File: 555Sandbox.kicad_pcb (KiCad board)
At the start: 2 copper layers, 64.6 x 37 mm, 33 parts, among them J1 VIN, J2 Piezo, Q1 2N7000, SW1 RESET, SW2 MODE, U1 NE555P, U2 LM3914N

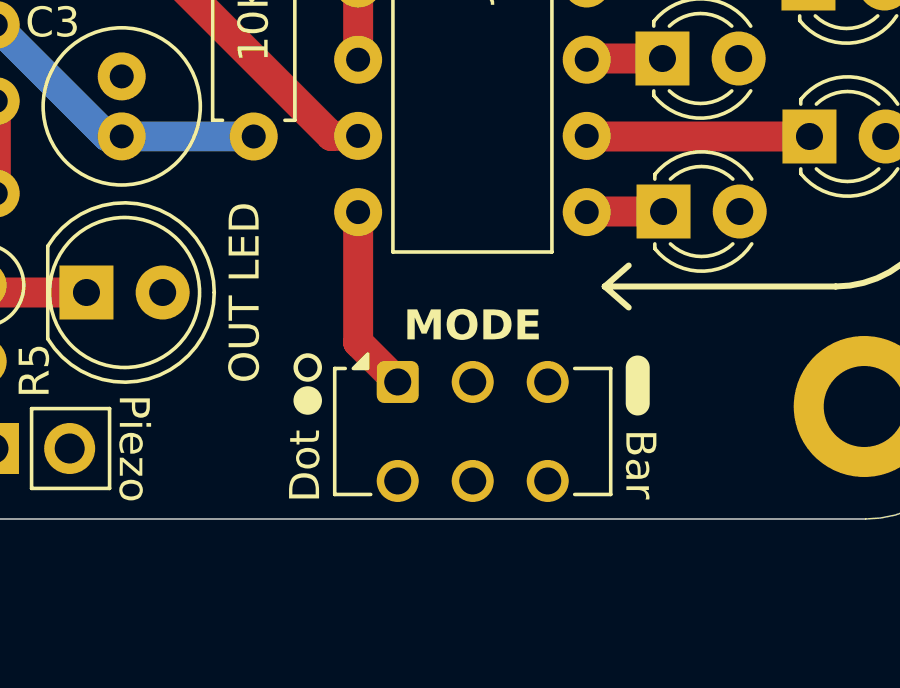
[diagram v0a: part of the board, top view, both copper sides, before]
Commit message: fix: mode switch footprint & silkscreen labels
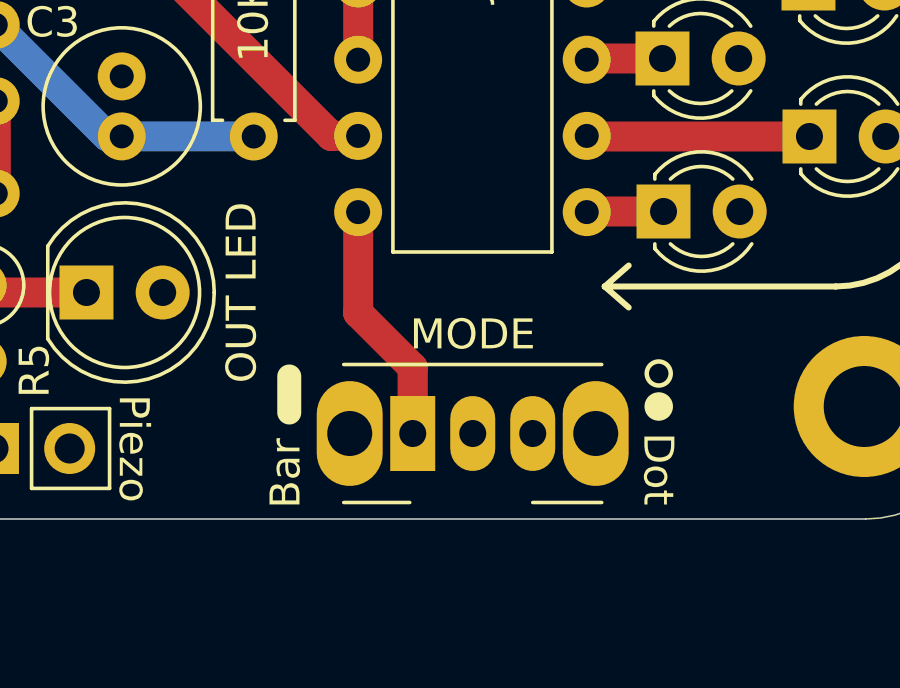
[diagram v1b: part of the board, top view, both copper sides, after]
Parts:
- SW2: footprint Button_Switch_THT:SW_CK_JS202011AQN_DPDT_Angled -> Button_Switch_THT:SW_Slide_SPDT_Angled_CK_OS102011MA1Q
- moved SW2 1.79 mm to (120.7, 98.4)
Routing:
- net Net-(SW2A-A): track 6.21 -> 8.13 mm

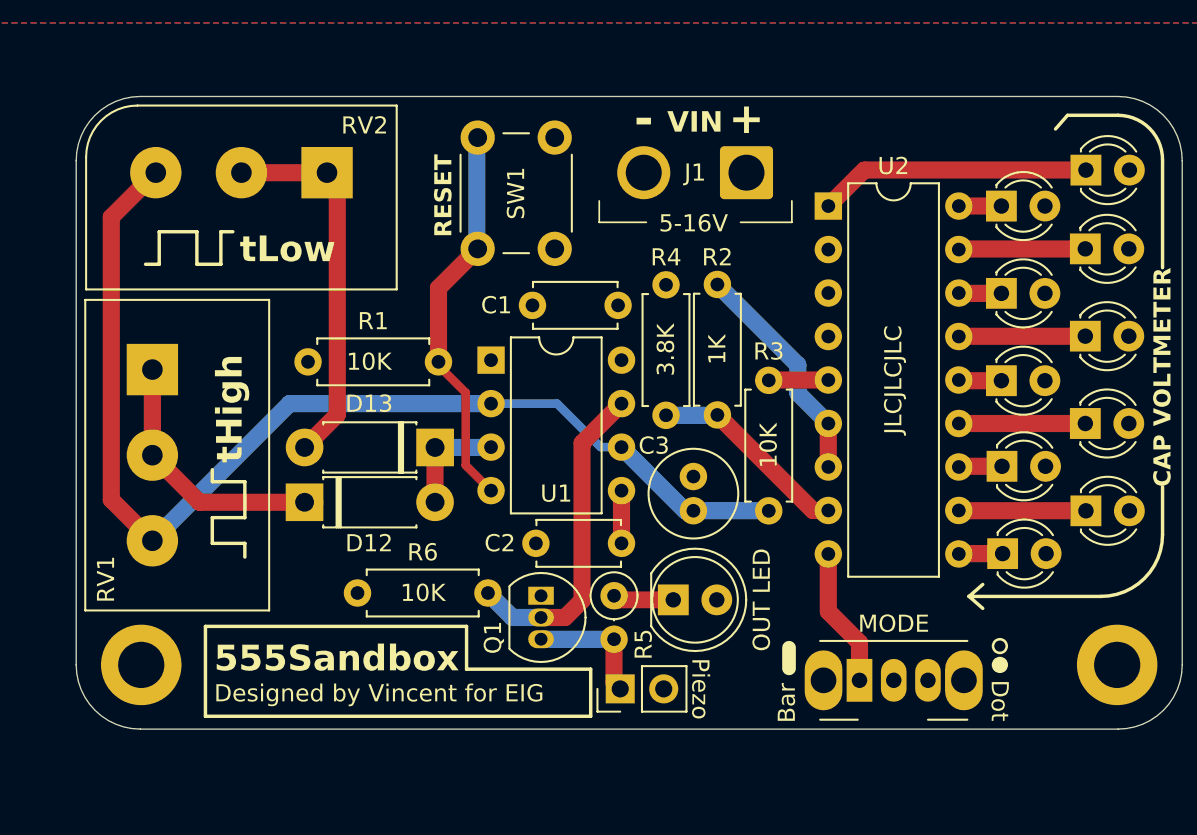
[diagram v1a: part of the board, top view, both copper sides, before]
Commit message: feat: update with separate freq and period adjustment
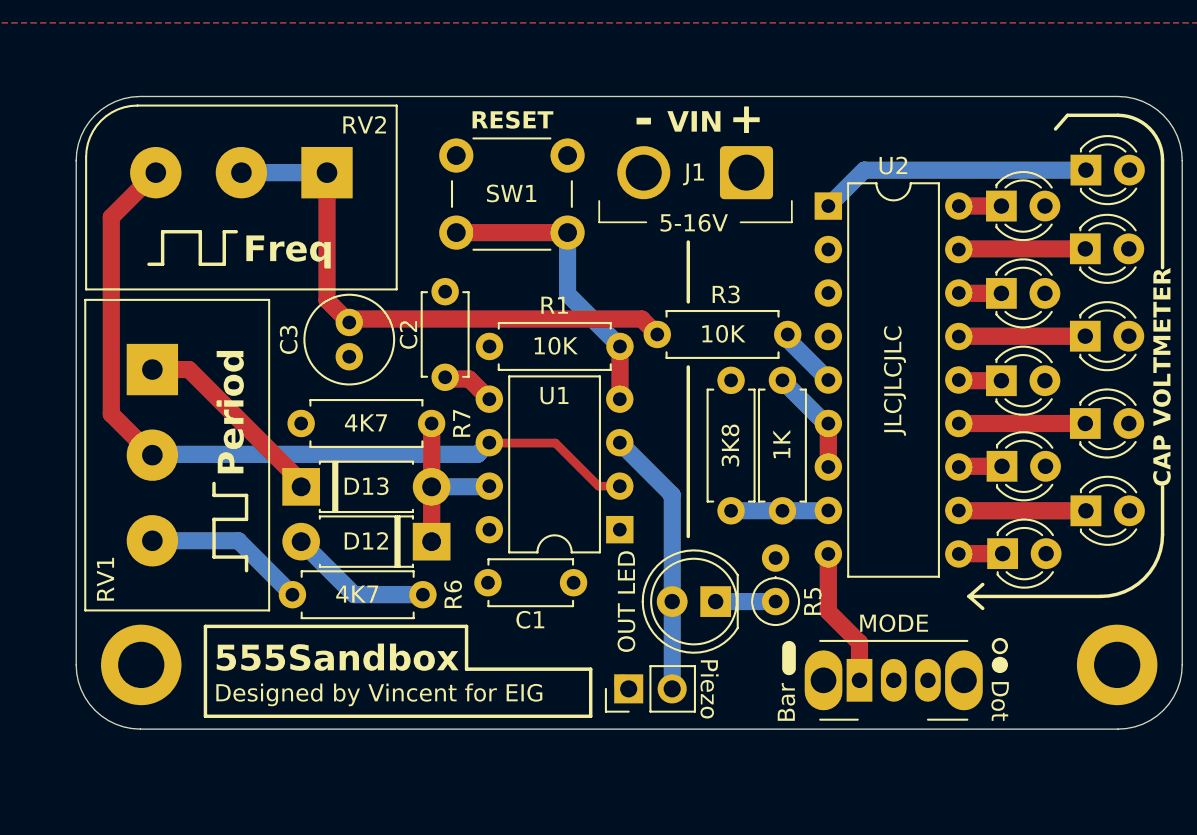
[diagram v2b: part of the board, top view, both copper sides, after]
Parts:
- removed Q1: 2N7000, Package_TO_SOT_THT:TO-92_Inline
- added R7: 4K7, Resistor_THT:R_Axial_DIN0207_L6.3mm_D2.5mm_P7.62mm_Horizontal, F.Cu at (88.1, 83.4)
- R4: value 3.8K -> 3K8
- R6: value 10K -> 4K7
- moved C3 22.9 mm to (90.9, 77.5), turned to -90 degrees
- moved C1 17.9 mm to (99.0, 92.7), turned to 0 degrees
- moved C2 14.1 mm to (96.5, 80.7), turned to 90 degrees
- moved U1 12.4 mm to (106.7, 89.6), turned to 180 degrees
- moved R3 12.2 mm to (108.9, 78.2), turned to 0 degrees
- moved R1 10.6 mm to (99.1, 78.9)
- moved R5 9.44 mm to (115.8, 93.8), turned to 90 degrees
- moved R2 6.77 mm to (116.2, 88.5)
- moved R4 6.75 mm to (113.2, 80.9)
- moved SW1 5.85 mm to (97.2, 67.8), turned to 0 degrees
- moved D13 5.50 mm to (95.7, 90.3)
- moved R6 3.82 mm to (95.2, 93.4), turned to 180 degrees
- moved D1 2.48 mm to (112.3, 93.8), turned to 180 degrees
- moved D12 0.92 mm to (88.1, 87.1)
- moved J2 0.50 mm to (107.2, 98.9)
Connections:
- C3 pad 1: /TRIG -> /VCAP
- D1 pad 2: VCC -> /OUT
- D12 pad 2: Net-(D12-A) -> /DIS
- D13 pad 1: Net-(D12-A) -> /DIS
- J2 pad 1: /OUT -> GND
- J2 pad 2: VCC -> /OUT
- R3 pad 1: /TRIG -> /VCAP
- R5 pad 2: /OUT -> GND
- R6 pad 1: VCC -> Net-(D13-A)
- R6 pad 2: /OSC_OUT -> Net-(R6-Pad2)
- RV1 pad 2: Net-(D12-K) -> /TRIG
- RV1 pad 3: /TRIG -> Net-(R6-Pad2)
- RV2 pad 1: Net-(D13-A) -> /VCAP
- RV2 pad 2: Net-(D13-A) -> /VCAP
- U1 pad 3: Net-(D12-A) -> /OUT
- U1 pad 7: /OSC_OUT -> /DIS
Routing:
- net /VCAP: track 0.00 -> 32.7 mm
- net /OSC_OUT: track 19.0 -> 0.00 mm
- net /TRIG: track 65.5 -> 47.2 mm
- net Net-(D13-A): track 22.1 -> 8.39 mm
- net /DIS: track 0.00 -> 10.3 mm
- net Net-(R6-Pad2): track 0.00 -> 9.48 mm
- net /OUT: track 7.31 -> 15.6 mm
- net /Voltage Meter/REF: track 13.3 -> 6.26 mm
- net /Voltage Meter/REFADJ: track 11.8 -> 5.72 mm
- net Net-(D12-A): track 5.88 -> 0.00 mm
- net /RST: track 22.9 -> 17.5 mm
- net Net-(D12-K): track 15.6 -> 11.4 mm
- net GND: track 0.00 -> 0.51 mm
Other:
- board text added: "Freq"
- board text added: "Period"
- board text removed: "tHigh"
- board text removed: "tLow"

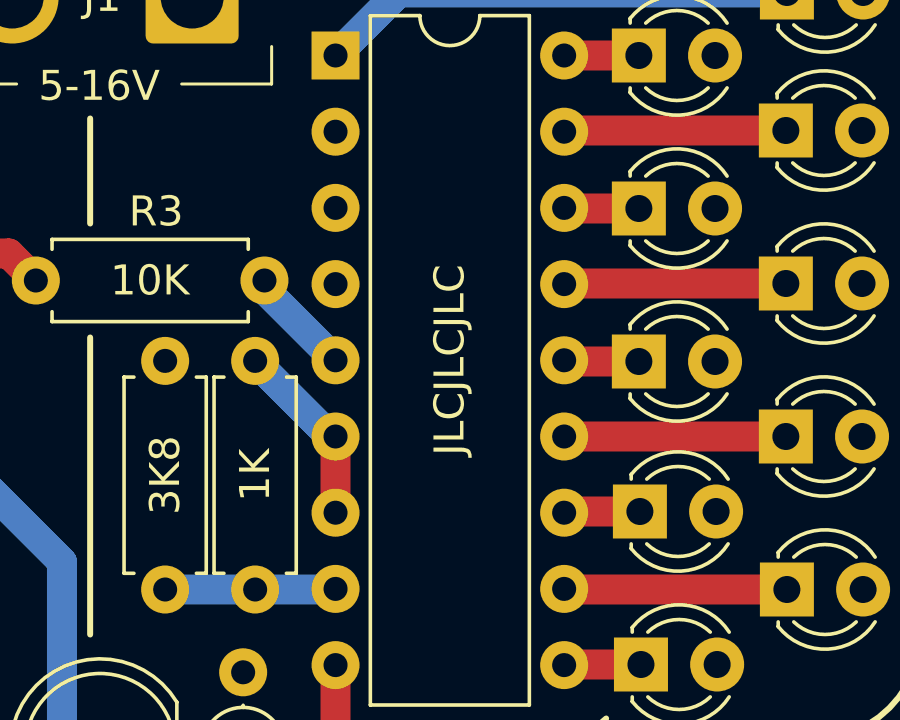
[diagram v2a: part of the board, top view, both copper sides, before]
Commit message: fix: JLC text
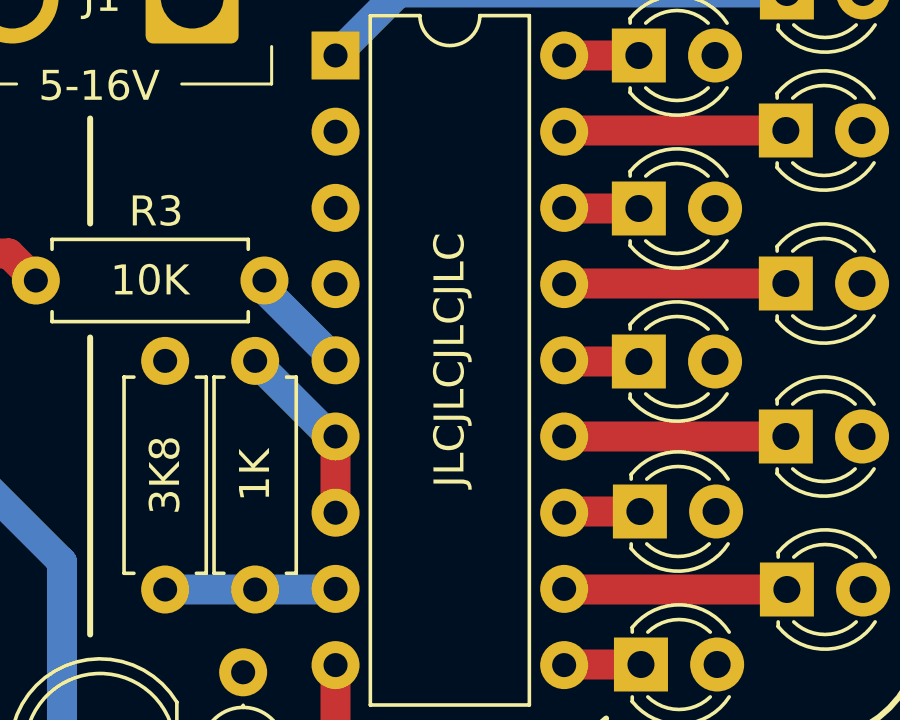
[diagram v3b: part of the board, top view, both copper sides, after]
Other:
- board text added: "JLCJLCJLCJLC"
- board text removed: "JLCJLCJLC"
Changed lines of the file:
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@@
 		)
 	)
-	(gr_text "JLCJLCJLC"
+	(gr_text "JLCJLCJLCJLC"
 		(at 122.68 80.85 90)
 		(layer "F.SilkS")

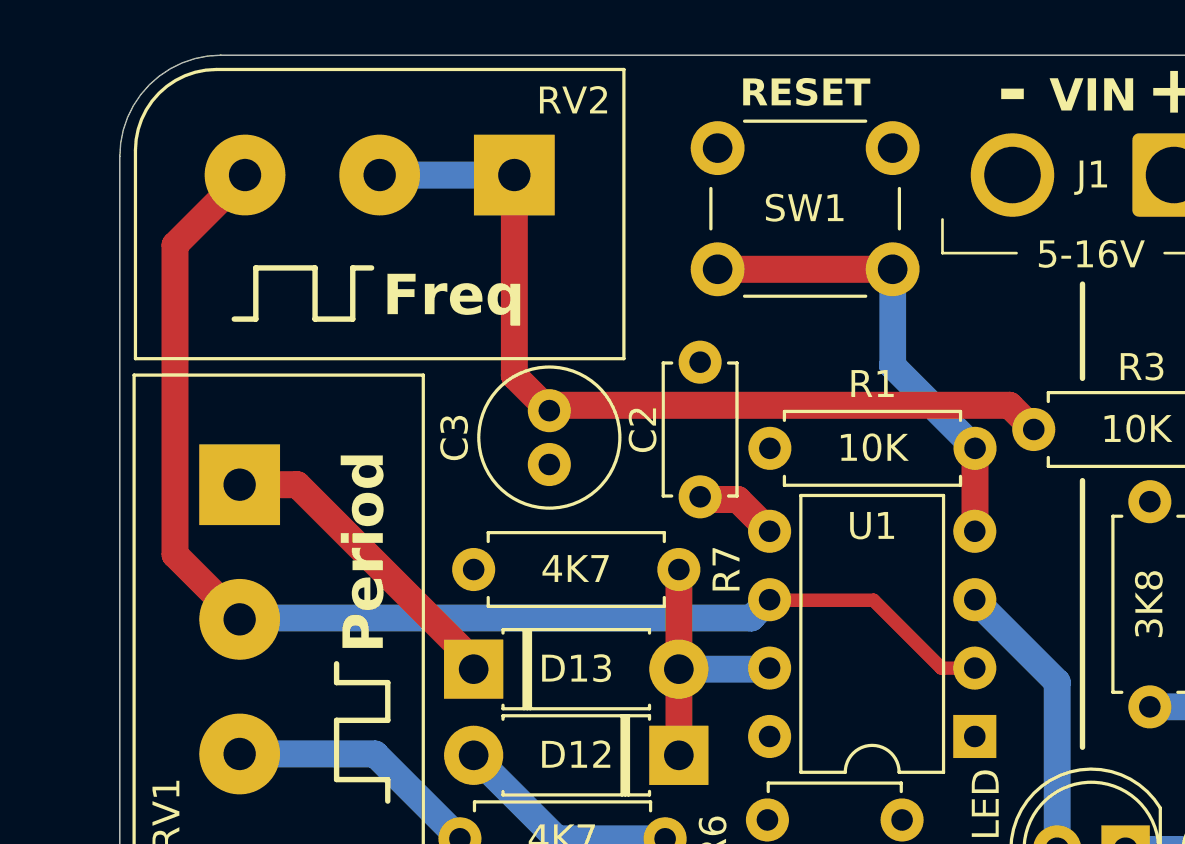
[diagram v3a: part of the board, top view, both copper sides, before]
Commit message: fix: connect trig to cap directly
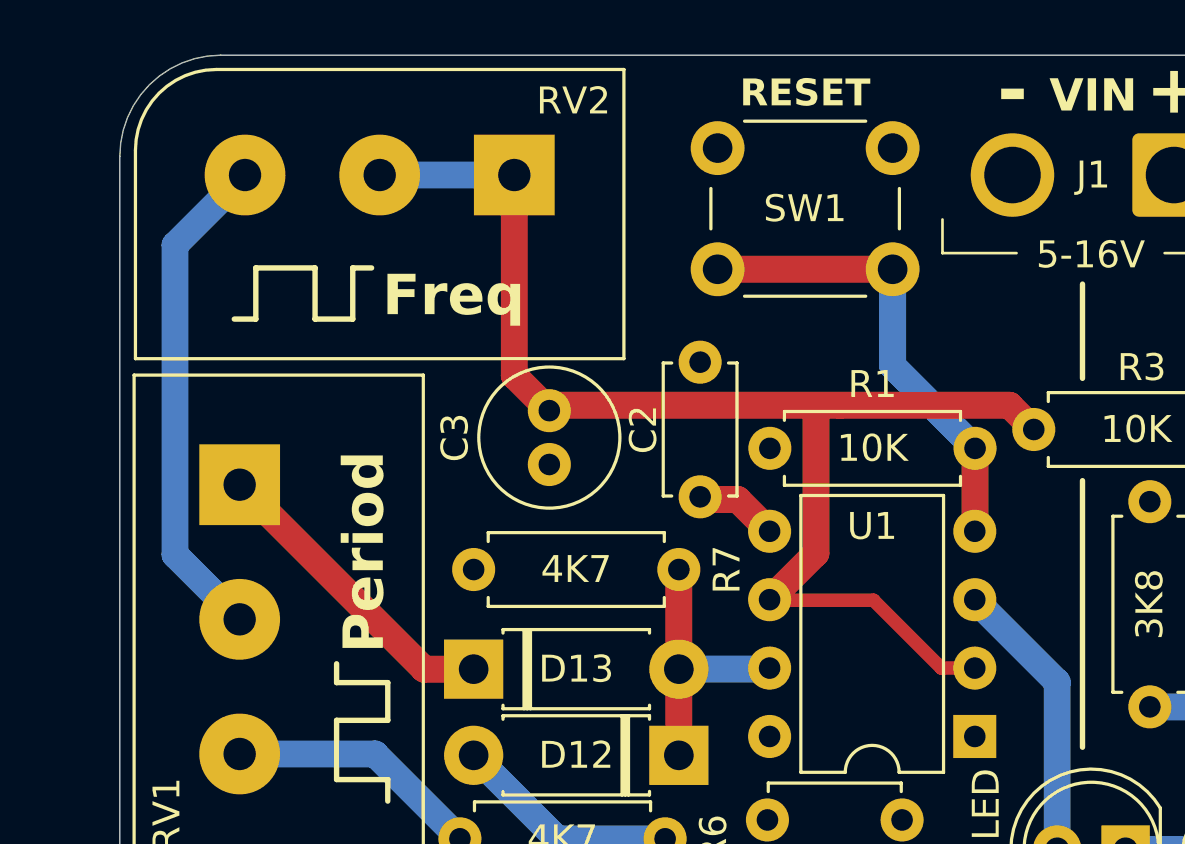
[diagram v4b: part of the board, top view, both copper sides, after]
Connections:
- C3 pad 1: /VCAP -> /TRIG
- R3 pad 1: /VCAP -> /TRIG
- RV1 pad 2: /TRIG -> Net-(RV1-Pad2)
- RV2 pad 1: /VCAP -> /TRIG
- RV2 pad 2: /VCAP -> /TRIG
- RV2 pad 3: /TRIG -> Net-(RV1-Pad2)
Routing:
- net /VCAP: track 32.7 -> 0.00 mm
- net Net-(RV1-Pad2): track 0.00 -> 18.6 mm
- net /TRIG: track 47.2 -> 49.3 mm
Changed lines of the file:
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@@
 	(net 25 "Net-(SW2A-A)")
 	(net 26 "Net-(R6-Pad2)")
-	(net 27 "/VCAP")
+	(net 27 "Net-(RV1-Pad2)")
 	(footprint "Package_DIP:DIP-8_W7.62mm"
 		(layer "F.Cu")
@@
 		(tags "LED diameter 5.0mm 2 pins")
 		(property "Reference" "D1"
-			(at 5.24 0 270)
+			(at 5.24 0 -90)
 			(layer "F.SilkS")
 			(hide yes)
@@
 		)
 		(property "Value" "OUT LED"
-			(at 5.175 0 270)
+			(at 5.175 0 -90)
 			(layer "F.SilkS")
 			(effects
@@
 		(tags "tact sw push 6mm")
 		(property "Reference" "SW1"
-			(at 3.25 2.25 360)
+			(at 3.25 2.25 0)
 			(layer "F.SilkS")
 			(effects
@@
 		)
 		(fp_text user "${REFERENCE}"
-			(at 3.25 2.25 360)
+			(at 3.25 2.25 0)
 			(layer "F.Fab")
 			(hide yes)
@@
 			(layers "*.Cu" "*.Mask")
 			(remove_unused_layers no)
-			(net 27 "/VCAP")
+			(net 4 "/TRIG")
 			(pintype "passive")
 		)
@@
 		(tags "Resistor Axial_DIN0207 series Axial Vertical pin pitch 2.54mm 0.25W = 1/4W length 6.3mm diameter 2.5mm")
 		(property "Reference" "R5"
-			(at 0 2.2 270)
+			(at 0 2.2 -90)
 			(layer "F.SilkS")
 			(effects
@@
 		)
 		(property "Value" "200"
-			(at 1.27 2.37 270)
+			(at 1.27 2.37 -90)
 			(layer "F.Fab")
 			(effects
@@
 		)
 		(fp_text user "${REFERENCE}"
-			(at 1.27 -2.37 270)
+			(at 1.27 -2.37 -90)
 			(layer "F.Fab")
 			(effects
@@
 		)
 		(property "Value" "10K"
-			(at 3.8 0 360)
+			(at 3.8 0 0)
 			(layer "F.SilkS")
 			(effects
@@
 		)
 		(fp_text user "${REFERENCE}"
-			(at 3.81 0 360)
+			(at 3.81 0 0)
 			(layer "F.Fab")
 			(effects
@@
 			(layers "*.Cu" "*.Mask")
 			(remove_unused_layers no)
-			(net 27 "/VCAP")
+			(net 4 "/TRIG")
 			(pintype "passive")
 		)
@@
 		)
 		(fp_text user "${REFERENCE}"
-			(at 3.81 0 360)
+			(at 3.81 0 0)
 			(layer "F.Fab")
 			(effects
@@
 		(tags "C Disc series Radial pin pitch 5.00mm  diameter 4.7mm width 2.5mm Capacitor")
 		(property "Reference" "C2"
-			(at 2.5 -2.1 270)
+			(at 2.5 -2.1 -90)
 			(layer "F.SilkS")
 			(effects
@@
 		)
 		(property "Value" "0.1uF"
-			(at 2.5 2.5 270)
+			(at 2.5 2.5 -90)
 			(layer "F.Fab")
 			(effects
@@
 		)
 		(fp_text user "${REFERENCE}"
-			(at 2.5 0 270)
+			(at 2.5 0 -90)
 			(layer "F.Fab")
 			(effects
@@
 		(tags "C Disc series Radial pin pitch 5.00mm  diameter 4.7mm width 2.5mm Capacitor")
 		(property "Reference" "C1"
-			(at 2.5 2.2 360)
+			(at 2.5 2.2 0)
 			(layer "F.SilkS")
 			(effects
@@
 		)
 		(property "Value" "0.1uF"
-			(at 2.5 2.5 360)
+			(at 2.5 2.5 0)
 			(layer "F.Fab")
 			(effects
@@
 		)
 		(fp_text user "${REFERENCE}"
-			(at 2.5 0 360)
+			(at 2.5 0 0)
 			(layer "F.Fab")
 			(effects
@@
 		(tags "Resistor Axial_DIN0207 series Axial Horizontal pin pitch 7.62mm 0.25W = 1/4W length 6.3mm diameter 2.5mm")
 		(property "Reference" "R1"
-			(at 3.81 -2.37 360)
+			(at 3.81 -2.37 0)
 			(layer "F.SilkS")
 			(effects
@@
 		)
 		(property "Value" "10K"
-			(at 3.81 0 360)
+			(at 3.81 0 0)
 			(layer "F.SilkS")
 			(effects
@@
 		)
 		(fp_text user "${REFERENCE}"
-			(at 3.81 0 360)
+			(at 3.81 0 0)
 			(layer "F.Fab")
 			(hide yes)
@@
 			(layers "*.Cu" "*.Mask")
 			(remove_unused_layers no)
-			(net 27 "/VCAP")
+			(net 4 "/TRIG")
 			(pinfunction "1")
 			(pintype "passive")
@@
 			(layers "*.Cu" "*.Mask")
 			(remove_unused_layers no)
-			(net 27 "/VCAP")
+			(net 4 "/TRIG")
 			(pinfunction "2")
 			(pintype "passive")
@@
 			(layers "*.Cu" "*.Mask")
 			(remove_unused_layers no)
-			(net 4 "/TRIG")
+			(net 27 "Net-(RV1-Pad2)")
 			(pinfunction "3")
 			(pintype "passive")
@@
 			(layers "*.Cu" "*.Mask")
 			(remove_unused_layers no)
-			(net 4 "/TRIG")
+			(net 27 "Net-(RV1-Pad2)")
 			(pinfunction "2")
 			(pintype "passive")
@@
 	)
 	(segment
+		(start 100.8 82.8)
+		(end 99.08 84.52)
+		(width 1)
+		(layer "F.Cu")
+		(net 4)
+	)
+	(segment
 		(start 105.46 87.06)
 		(end 102.94 84.54)
@@
 	)
 	(segment
-		(start 77 71.35)
-		(end 77 82.85)
+		(start 90.9 77.5)
+		(end 91.1 77.3)
 		(width 1)
 		(layer "F.Cu")
@@
 	)
 	(segment
-		(start 79.6 68.75)
-		(end 77 71.35)
+		(start 89.6 68.75)
+		(end 89.6 76.2)
 		(width 1)
 		(layer "F.Cu")
@@
 	)
 	(segment
-		(start 106.7 87.06)
-		(end 105.46 87.06)
-		(width 0.5)
+		(start 91.1 77.3)
+		(end 101.7 77.3)
+		(width 1)
 		(layer "F.Cu")
 		(net 4)
 	)
 	(segment
-		(start 77 82.85)
-		(end 79.4 85.25)
+		(start 100.8 77.3)
+		(end 100.8 82.8)
 		(width 1)
 		(layer "F.Cu")
@@
 	)
 	(segment
-		(start 79.4 85.25)
-		(end 79.45 85.2)
+		(start 101.7 77.3)
+		(end 107.99 77.3)
 		(width 1)
-		(layer "B.Cu")
+		(layer "F.Cu")
 		(net 4)
 	)
 	(segment
-		(start 98.4 85.2)
-		(end 99.08 84.52)
+		(start 107.99 77.3)
+		(end 108.89 78.2)
 		(width 1)
-		(layer "B.Cu")
+		(layer "F.Cu")
+		(net 4)
+	)
+	(segment
+		(start 106.7 87.06)
+		(end 105.46 87.06)
+		(width 0.5)
+		(layer "F.Cu")
+		(net 4)
+	)
+	(segment
+		(start 89.6 76.2)
+		(end 90.9 77.5)
+		(width 1)
+		(layer "F.Cu")
 		(net 4)
 	)
 	(segment
-		(start 79.45 85.2)
-		(end 98.4 85.2)
+		(start 84.6 68.75)
+		(end 89.6 68.75)
 		(width 1)
 		(layer "B.Cu")
@@
 	)
 	(segment
-		(start 81.54 80.25)
-		(end 79.4 80.25)
+		(start 88.09 87.1)
+		(end 86.25 87.1)
 		(width 1)
 		(layer "F.Cu")
@@
 	)
 	(segment
-		(start 88.09 86.8)
-		(end 81.54 80.25)
+		(start 86.25 87.1)
+		(end 79.4 80.25)
 		(width 1)
 		(layer "F.Cu")
@@
 	)
 	(segment
-		(start 91.1 77.3)
-		(end 107.99 77.3)
-		(width 1)
-		(layer "F.Cu")
-		(net 27)
-	)
-	(segment
-		(start 90.9 77.5)
-		(end 91.1 77.3)
-		(width 1)
-		(layer "F.Cu")
-		(net 27)
-	)
-	(segment
-		(start 89.6 68.75)
-		(end 89.6 76.2)
-		(width 1)
-		(layer "F.Cu")
-		(net 27)
-	)
-	(segment
-		(start 107.99 77.3)
-		(end 108.89 78.2)
+		(start 77 71.35)
+		(end 77 82.85)
 		(width 1)
-		(layer "F.Cu")
+		(layer "B.Cu")
 		(net 27)
 	)
 	(segment
-		(start 89.6 76.2)
-		(end 90.9 77.5)
+		(start 79.6 68.75)
+		(end 77 71.35)
 		(width 1)
-		(layer "F.Cu")
+		(layer "B.Cu")
 		(net 27)
 	)
 	(segment
-		(start 84.6 68.75)
-		(end 89.6 68.75)
+		(start 77 82.85)
+		(end 79.4 85.25)
 		(width 1)
 		(layer "B.Cu")
